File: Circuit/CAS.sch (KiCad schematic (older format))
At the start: 24 parts, among them P1 CONN_01X03, P2 USB_A, P3 CONN_01X03, P4 USB_OTG, P5 CONN_01X03, P6 USB_A, P7 CONN_01X03, P8 USB_OTG, Q1 2N2222/2N3904, Q2 2N3906, Q3 2N2222/2N3904, U1 PC817, U2 PC817

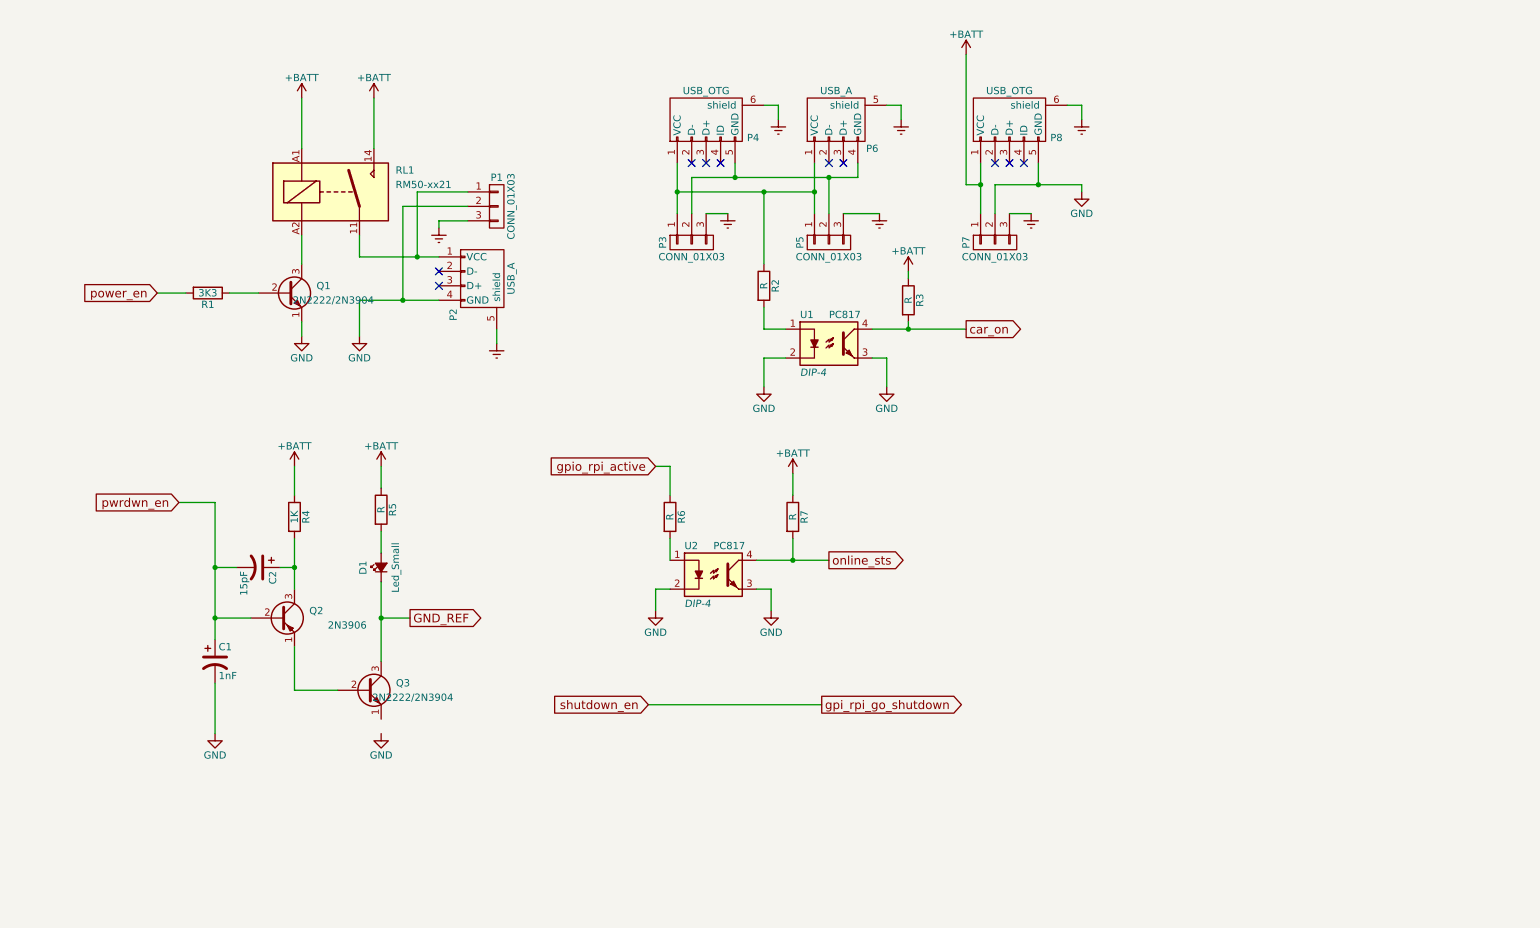
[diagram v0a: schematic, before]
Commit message: -Add full schematic for power circuit.
-Add BOM for power circuit.
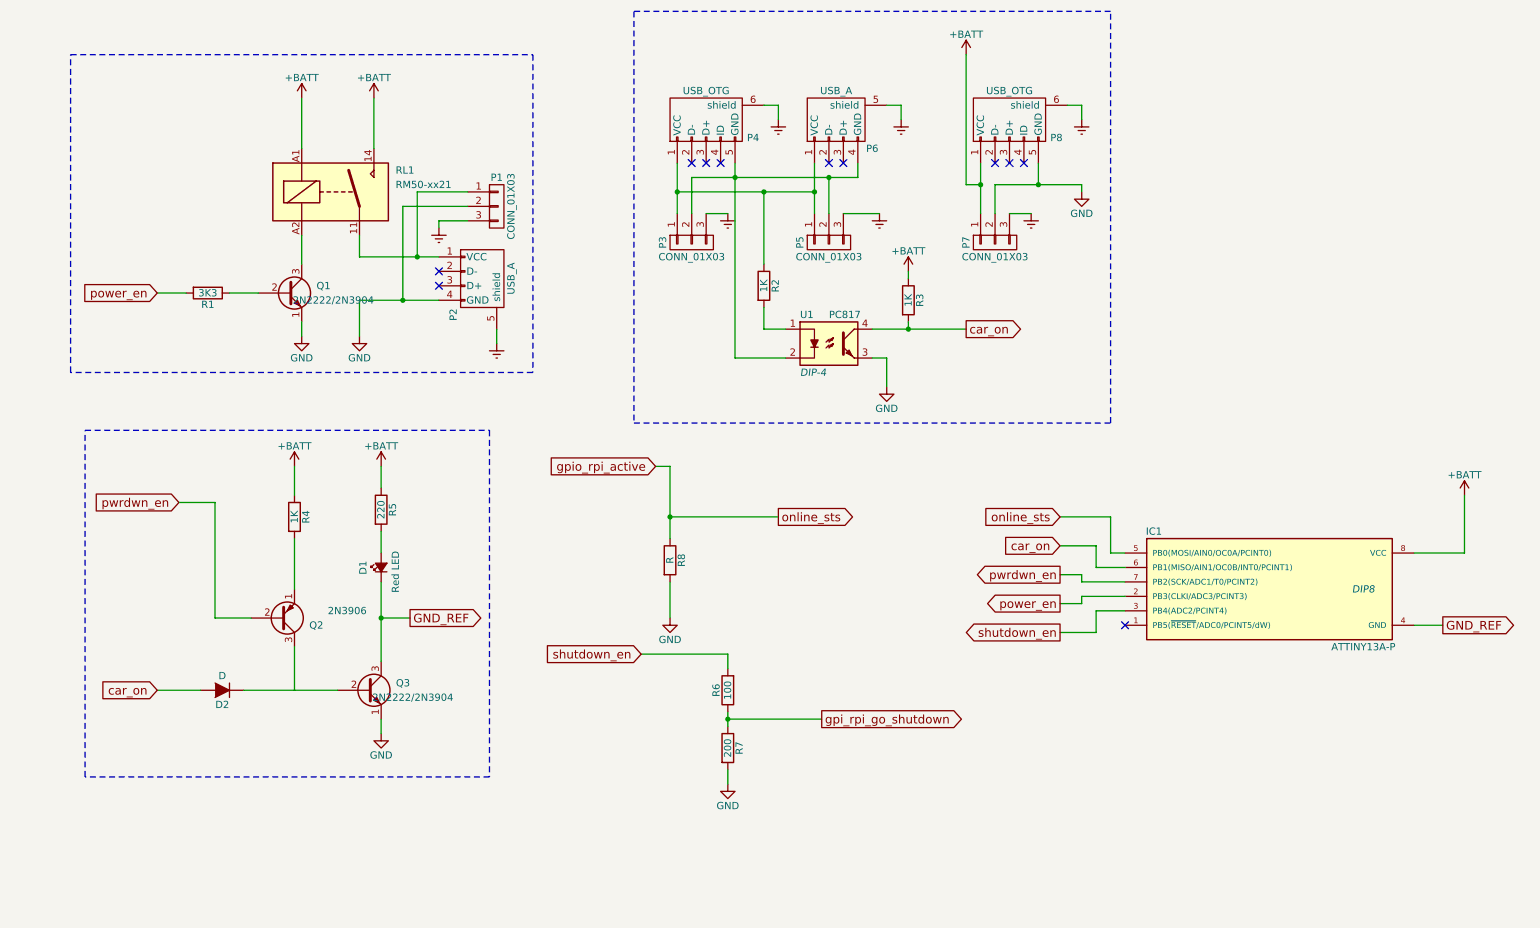
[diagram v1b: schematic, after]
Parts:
- removed C1: 1nF, symbol CP1
- removed C2: 15pF, symbol CP1
- removed U2: PC817, DIP-4, symbol PC817
- added D2: D, symbol D
- added IC1: ATTINY13A-P, DIP8, symbol ATTINY13A-P
- added R8: R, symbol R
- D1: value Led_Small -> Red LED
- R2, R3: value R -> 1K
- R5: value R -> 220
- R6: value R -> 100
- R7: value R -> 200
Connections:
- net online_sts is gone; now on net GND: R7.2
- net +BATT: now also IC1.8 (VCC); no longer R7.1
- net GND: now also Q3.1 (E), R8.2; no longer U1.2
- net GND_REF: now also IC1.4 (GND)
- net car_on: now also D2.2 (A), IC1.6 (PB1(MISO/AIN1/OC0B/INT0/PCINT1))
- net gpi_rpi_go_shutdown: now also R6.1, R7.1
- net gpio_rpi_active: now also IC1.5 (PB0(MOSI/AIN0/OC0A/PCINT0)), R8.1; no longer R6.1
- net power_en: now also IC1.2 (PB3(CLKI/ADC3/PCINT3))
- net pwrdwn_en: now also IC1.7 (PB2(SCK/ADC1/T0/PCINT2))
- net at P3.2 (P2), P4.5 (GND), P5.2 (P2)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: now also U1.2
- net at Q2.1 (E): now also R4.2; no longer Q3.2 (B)
- net at Q2.3 (C): no longer R4.2
- net shutdown_en: now reaches R6.2
- net shutdown_en: now also IC1.3 (PB4(ADC2/PCINT4))
- new net: D2.1 (K), Q3.2 (B)
- no-connect marks 10 -> 11

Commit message: Fix ERC error and remove redundant connection
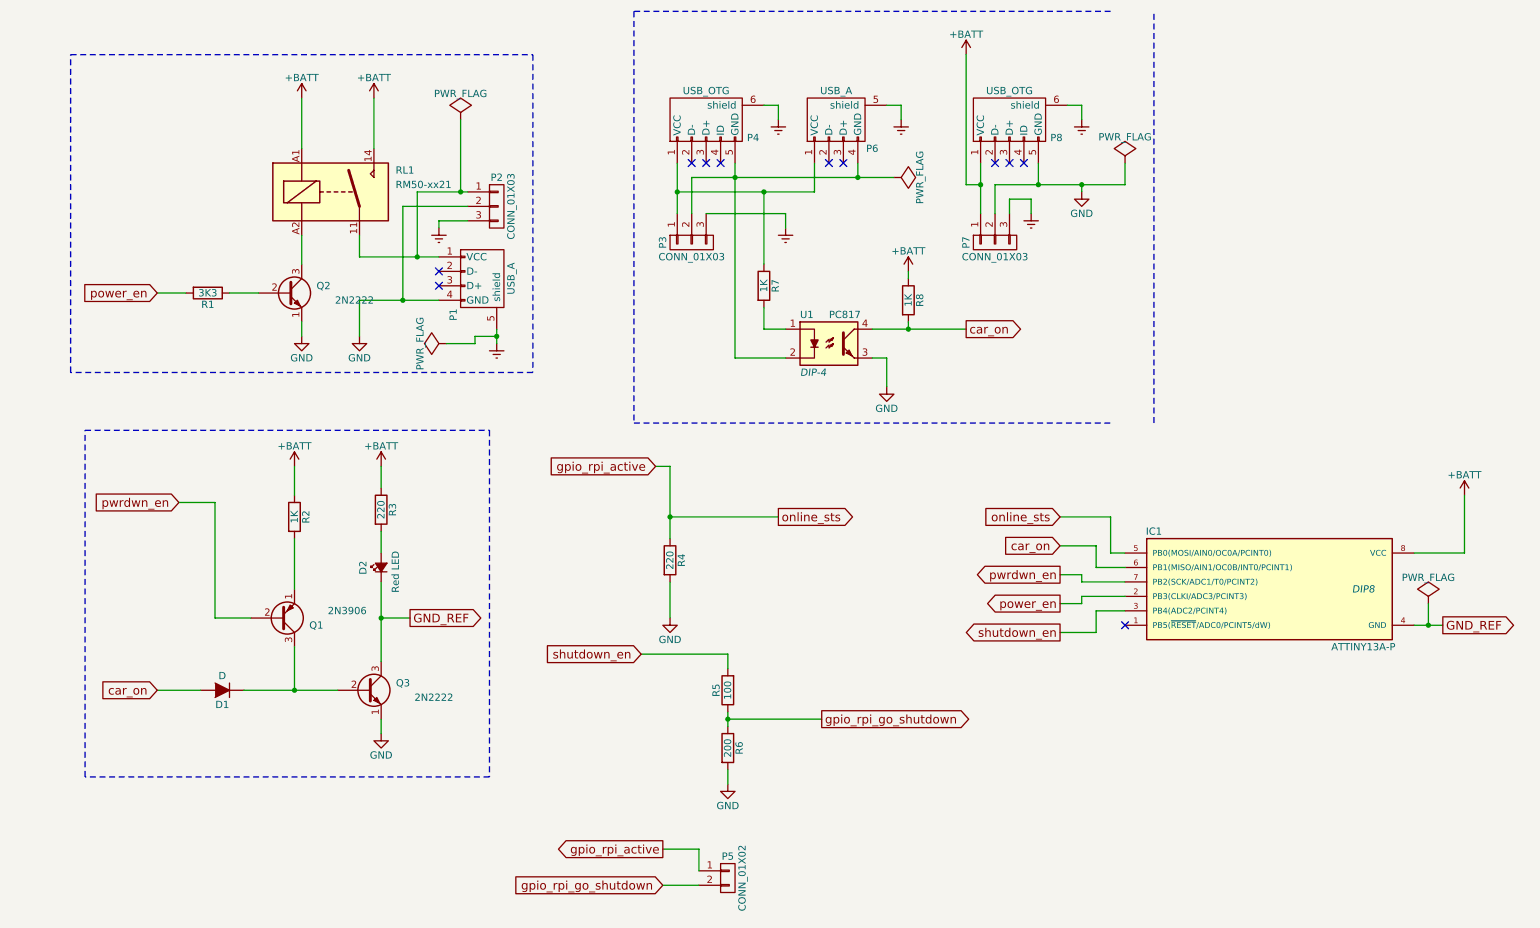
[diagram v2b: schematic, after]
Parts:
- removed P5: CONN_01X03, symbol CONN_01X03
- added P5: CONN_01X02, symbol CONN_01X02
- Q2: renamed from Q1; value 2N2222/2N3904 -> 2N2222
- Q3: value 2N2222/2N3904 -> 2N2222
- R4: renamed from R8; value R -> 220
- renumbered D2 to D1, D1 to D2, P2 to P1, P1 to P2, Q2 to Q1, R4 to R2, R5 to R3, R6 to R5, R7 to R6, R2 to R7, R3 to R8
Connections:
- net gpio_rpi_active: now also P5.1 (P1)
- net at Q1.3 (C): now also D1.1 (K), Q3.2 (B)
- net gpi_rpi_go_shutdown renamed gpio_rpi_go_shutdown
- net gpio_rpi_go_shutdown: now also P5.2 (P2)

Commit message: Add revision info and fix some minors
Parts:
- removed P1, P6: USB_A, symbol USB_A
- removed P4, P8: USB_OTG, symbol USB_OTG
- added P1, P6: USB_B, symbol USB_B
- added P4: CONN_01X03, symbol CONN_01X03
- added U2, U3: MICRO-B_USB, symbol MICRO-B_USB
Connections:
- net +BATT: now also U3.1 (VBUS)
- net Earth: now also P1.5 (shield), P4.3 (P3), P6.5 (shield)
- net GND: now also P1.4 (GND), U3.5 (GND)
- net at P2.1 (P1), RL1.11: now also P1.1 (VCC)
- net at P3.1 (P1), R7.1: now also P4.1 (P1), P6.1 (VCC), U2.1 (VBUS)
- net at P3.2 (P2), U1.2: now also P4.2 (P2), P6.4 (GND), U2.5 (GND)

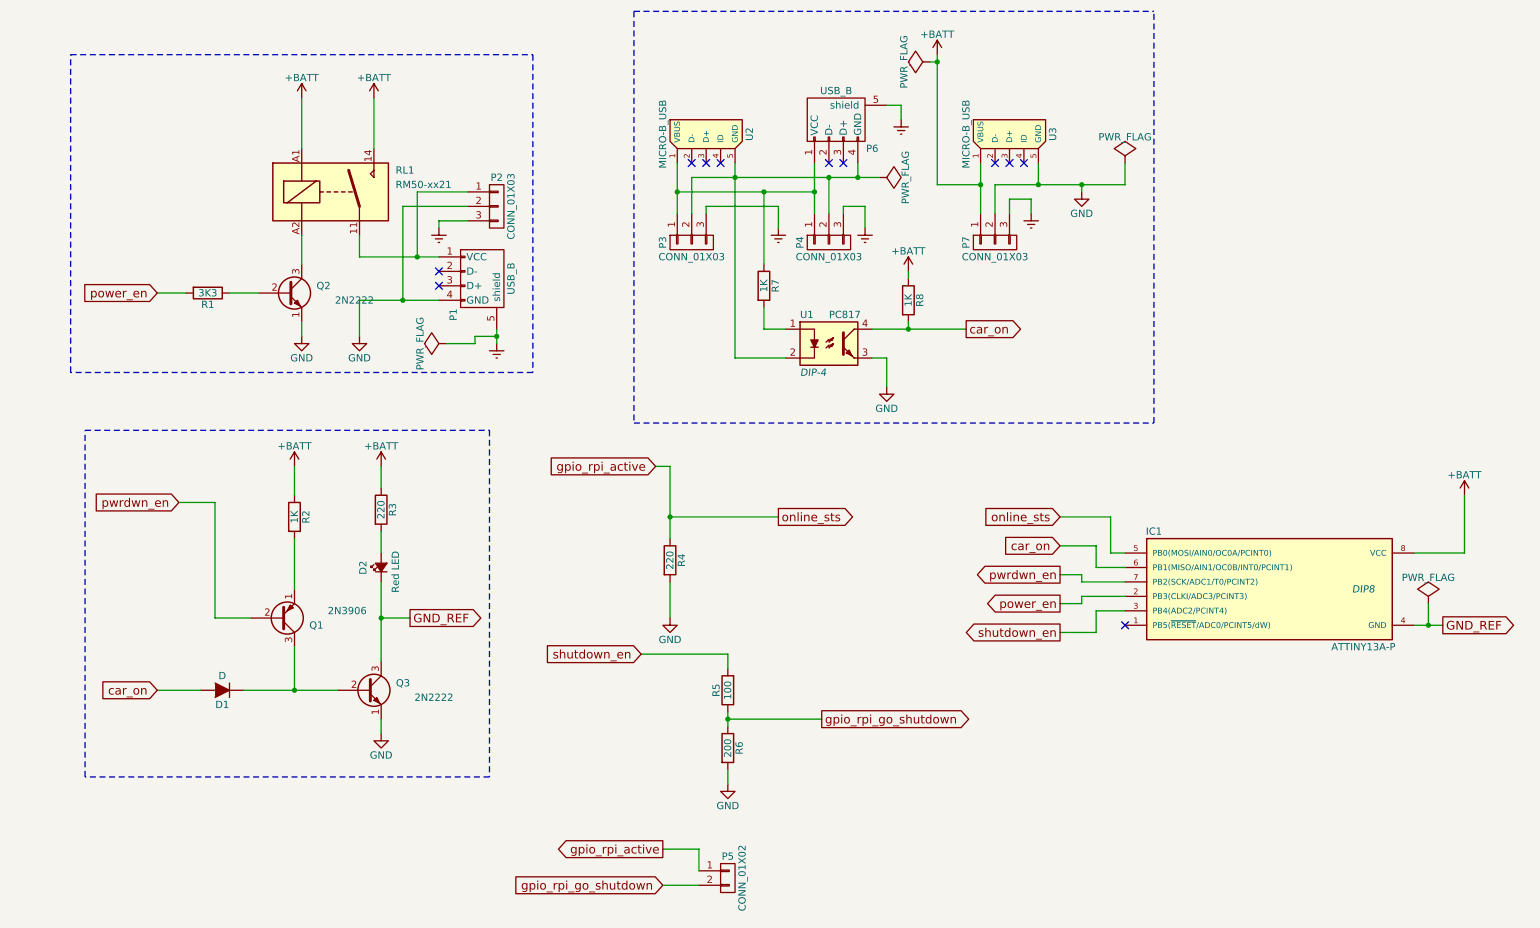
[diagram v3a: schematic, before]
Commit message: Add trial firmware for power management unit
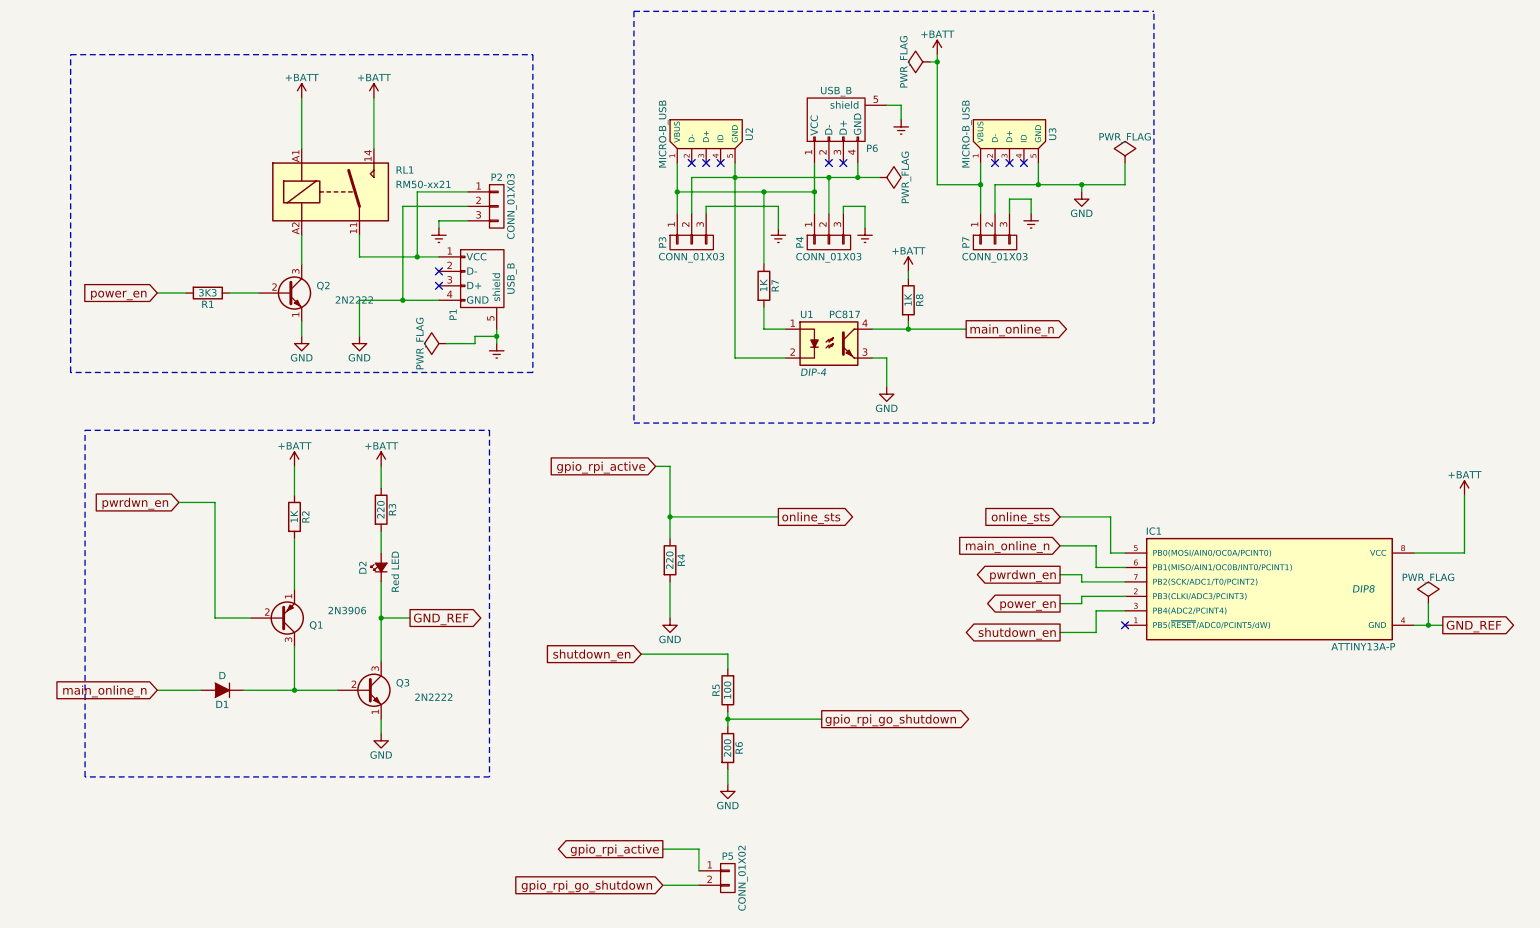
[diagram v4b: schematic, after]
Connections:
- net car_on renamed main_online_n
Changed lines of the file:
@@
 	6350 2800 7000 2800
 Text GLabel 7000 2800 2    60   Output ~ 0
-car_on
+main_online_n
 Connection ~ 6600 2800
 Text GLabel 1550 4000 0    60   Input ~ 0
@@
 	2950 5500 2950 5600
 Text GLabel 1400 5300 0    60   Input ~ 0
-car_on
+main_online_n
 Wire Notes Line
 	3700 5900 900  5900
@@
 online_sts
 Text GLabel 7650 4300 0    60   Input ~ 0
-car_on
+main_online_n
 Text GLabel 7650 4500 0    60   Output ~ 0
 pwrdwn_en

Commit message: Corrected power circuit and firmware
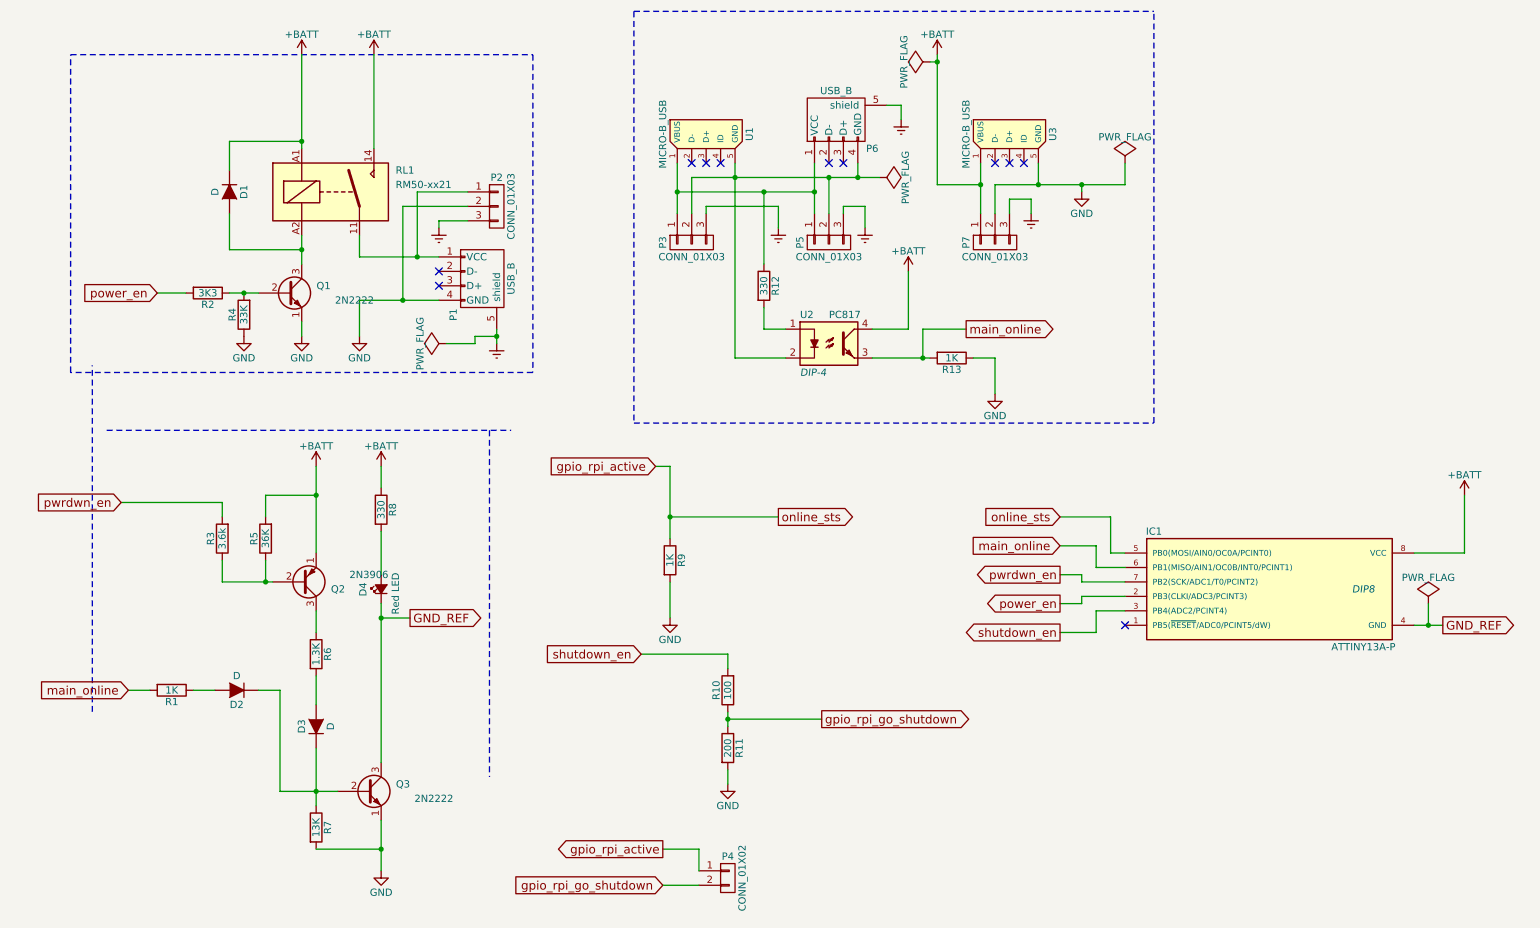
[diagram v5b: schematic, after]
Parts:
- added D2, D3: D, symbol D
- added R1: 1K, symbol R
- added R4: 33K, symbol R
- added R5: 36K, symbol R
- added R6: 1.3K, symbol R
- added R7: 13K, symbol R
- R12: renamed from R7; value 1K -> 330
- R3: renamed from R2; value 1K -> 3.6k
- R8: renamed from R3; value 220 -> 330
- R9: renamed from R4; value 220 -> 1K
- renumbered D2 to D4, P5 to P4, P4 to P5, Q2 to Q1, Q1 to Q2, R5 to R10, R6 to R11, R8 to R13, R1 to R2, U2 to U1, U1 to U2
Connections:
- net +BATT: now also D1.1 (K), Q2.1 (E), U2.4, R5.2; no longer R13.1, R3.1
- net GND: now also R13.1, R4.1, R7.2; no longer U2.3
- net pwrdwn_en: now also R3.2; no longer Q2.2 (B)
- net at Q1.3 (C), RL1.A2: now also D1.2 (A)
- net at Q1.2 (B), R2.1: now also R4.2
- net main_online_n renamed main_online
- net main_online: now also U2.3, R1.2; no longer D1.2 (A), U2.4
- new net: Q2.2 (B), R3.1, R5.1
- new net: Q2.3 (C), R6.1
- new net: D2.1 (K), D3.1 (K), Q3.2 (B), R7.1
- new net: D3.2 (A), R6.2
- new net: D2.2 (A), R1.1
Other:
- moved on the sheet: D4, Q2, Q3, R13, R3
